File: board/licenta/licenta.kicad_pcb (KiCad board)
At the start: 2 copper layers, 33.8 x 36.1 mm, 64 parts, among them IC3 SAMACSYS_PARTS_BMI085, J1 SAMACSYS_PARTS_USB4110-GF-A, J2 SAMACSYS_PARTS_112A-TAAR-R03_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, Q1 ESP32_WROVER_SPARKFUN-DISCRET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, Q2 2N7002, SW1 SW_Push, SW2 SW_Push, SW3 SW_Push, SW6 SW_Push, U2 ESP32_WROVER_SPARKFUN-IC-POWE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

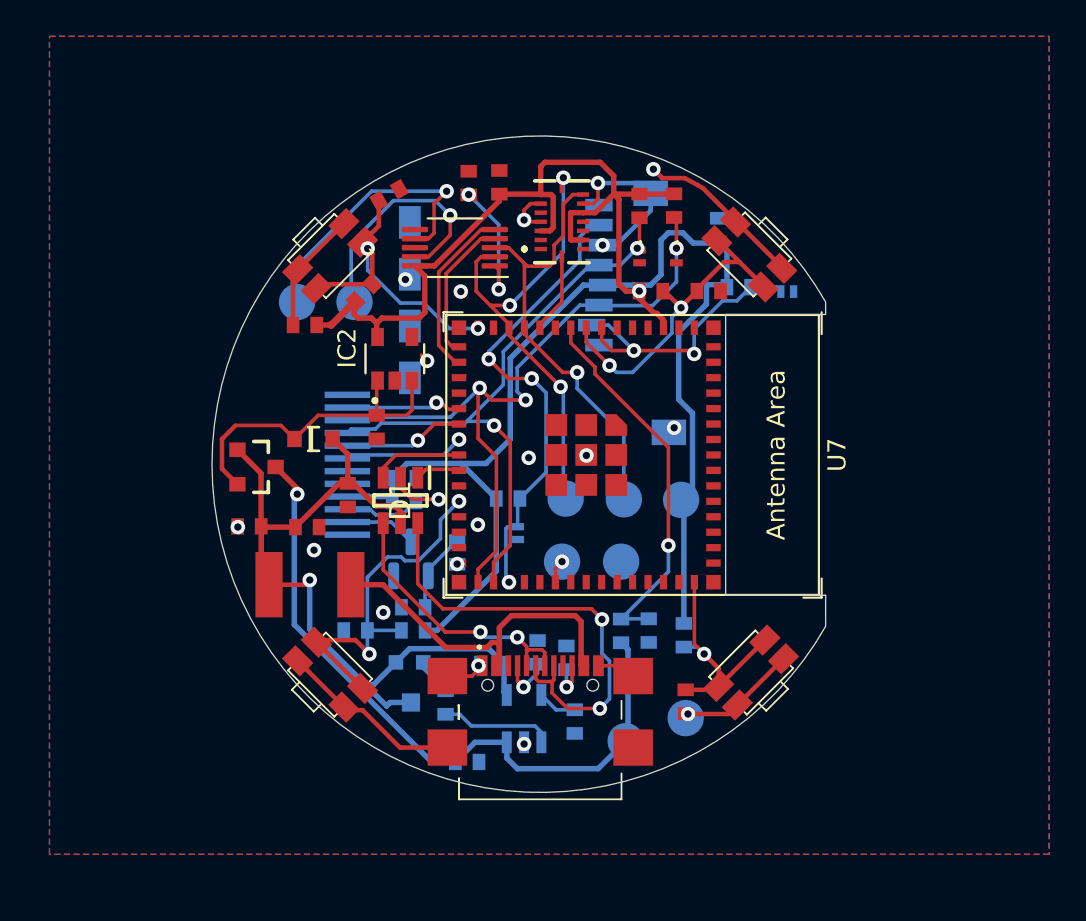
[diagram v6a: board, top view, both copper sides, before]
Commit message: Update board and schematic
This commit adds the following modifications:
- SDA and SCL pull-ups
- 100nF debounce capacitors for buttons
- vias tweaks to not come out of pads
- connect one button to be used both as BOOT and GPIO
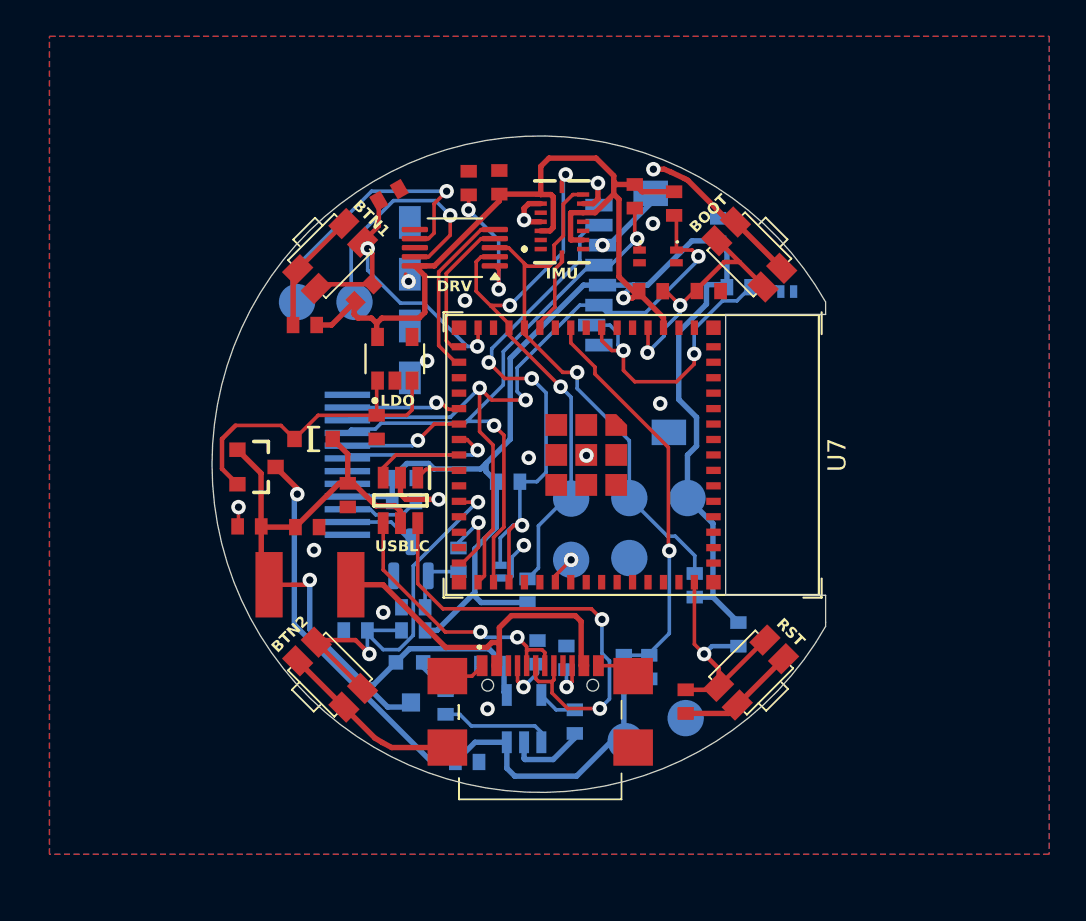
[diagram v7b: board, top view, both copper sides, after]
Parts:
- added R_SCL1: 4k7, mini_iot:ESP32_WROVER_EAGLE-LTSPICE_R0402, B.Cu at (126.3, 90.5)
- added R_SDA1: 4k7, mini_iot:ESP32_WROVER_EAGLE-LTSPICE_R0402, B.Cu at (135.5, 90.2)
- C3, C4, C5, C7: value 1uF -> 100nF
- moved R1_BTN4 3.00 mm to (137.9, 92.9)
- moved D6 2.33 mm to (124.8, 89.5)
- moved R6_ESP1 2.01 mm to (133.0, 94.7)
- moved R5_ESP1 2.00 mm to (131.6, 94.7)
- moved R4 0.93 mm to (125.2, 84.5)
- moved R2 0.59 mm to (132.2, 68.8)
- moved TP6 0.51 mm to (128.7, 88.8)
- moved TP7 0.49 mm to (131.9, 88.7)
- moved R1_ESP2 0.41 mm to (122.5, 88.8), turned to -90 degrees
- moved TP3 0.36 mm to (135.1, 85.4)
- moved TP4 0.31 mm to (131.9, 85.4)
- moved TP5 0.30 mm to (128.7, 85.4)
- moved R3 0.11 mm to (134.4, 69.2)
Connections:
- C4 pad 2: /BUTTON_2 -> /BOOT
- C5 pad 2: /BUTTON_3 -> /BUTTON_2
- R1_BTN1 pad 1: /BUTTON_2 -> /BOOT
- R1_BTN2 pad 1: /BUTTON_3 -> /BUTTON_2
- SW1 pad 2: /BUTTON_2 -> /BOOT
- SW2 pad 2: /BUTTON_3 -> /BUTTON_2
- U7 pad 26: /BUTTON_3 -> /BUTTON_2
- U7 pad 4: unconnected-(U7-GPIO0/BOOT-Pad4) -> /BOOT
- U7 pad 8: /BUTTON_2 -> unconnected-(U7-GPIO4/TOUCH4/ADC1_CH3-Pad8)
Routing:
- net /BUTTON_3: track 20.6 -> 0.00 mm, vias 2 -> 0
- net /BOOT: track 0.00 -> 14.1 mm, vias 0 -> 2
- net GND: track 53.8 -> 60.5 mm, vias 18 -> 17
- net /SCL: track 26.0 -> 32.0 mm
- net /SDA: track 24.2 -> 30.2 mm
- net /BUTTON_2: track 18.0 -> 23.5 mm
- net /3V3: track 113.7 -> 118.7 mm
- net /PIN_LED: track 0.14 -> 4.70 mm
- net /MISO: track 25.8 -> 29.3 mm
- net /TFT_DC: track 6.57 -> 8.62 mm
- net /SS_SD: track 16.2 -> 18.2 mm
- net /MOSI: track 38.8 -> 40.3 mm
- net /VBAT: track 38.4 -> 36.9 mm
- net /ADC_BAT: track 20.9 -> 22.3 mm
- net /BUTTON_1: track 16.5 -> 17.9 mm
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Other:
- board text added: "BOOT"
- board text added: "BTN1"
- board text added: "BTN2"
- board text added: "DISP"
- board text added: "DRV"
- board text added: "IMU"
- board text added: "LDO"
- board text added: "MCP"
- board text added: "RST"
- board text added: "USBLC"
